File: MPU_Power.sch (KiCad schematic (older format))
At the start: 45 parts, among them U1 STM32MP151AAB3

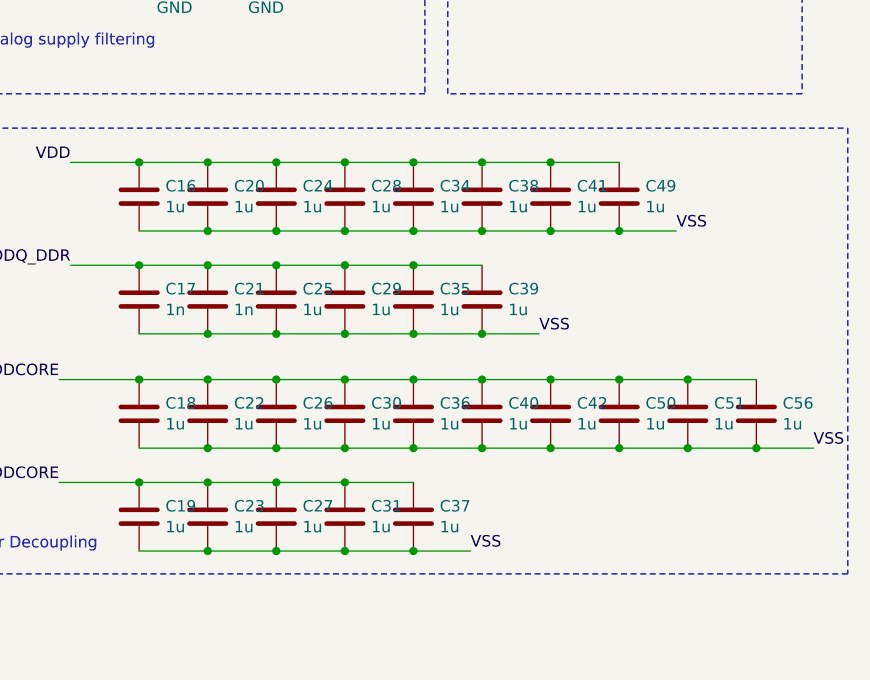
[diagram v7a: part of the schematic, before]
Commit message: Update jtag connector to swd
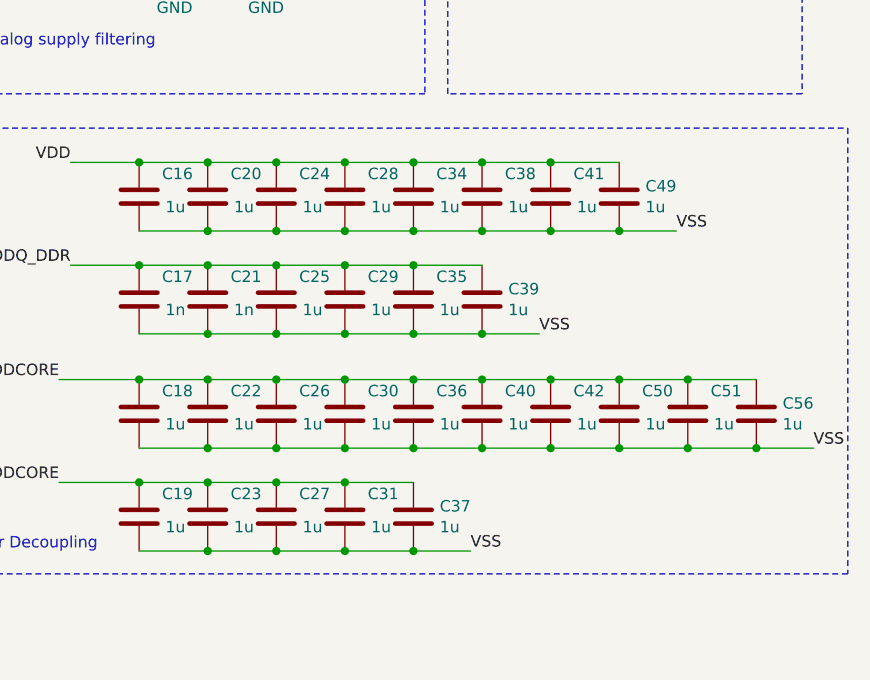
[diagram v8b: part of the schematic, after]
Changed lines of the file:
@@
 U 1 1 60A31F57
 P 8050 5700
-F 0 "C18" H 8165 5746 50  0000 L CNN
+F 0 "C18" H 8150 5800 50  0000 L CNN
 F 1 "1u" H 8165 5655 50  0000 L CNN
 F 2 "Capacitor_SMD:C_0603_1608Metric" H 8088 5550 50  0001 C CNN
@@
 U 1 1 60A5393A
 P 8350 5700
-F 0 "C22" H 8465 5746 50  0000 L CNN
+F 0 "C22" H 8450 5800 50  0000 L CNN
 F 1 "1u" H 8465 5655 50  0000 L CNN
 F 2 "Capacitor_SMD:C_0603_1608Metric" H 8388 5550 50  0001 C CNN
@@
 U 1 1 60A5C6B0
 P 8650 5700
-F 0 "C26" H 8765 5746 50  0000 L CNN
+F 0 "C26" H 8750 5800 50  0000 L CNN
 F 1 "1u" H 8765 5655 50  0000 L CNN
 F 2 "Capacitor_SMD:C_0603_1608Metric" H 8688 5550 50  0001 C CNN
@@
 U 1 1 60A653E0
 P 8950 5700
-F 0 "C30" H 9065 5746 50  0000 L CNN
+F 0 "C30" H 9050 5800 50  0000 L CNN
 F 1 "1u" H 9065 5655 50  0000 L CNN
 F 2 "Capacitor_SMD:C_0603_1608Metric" H 8988 5550 50  0001 C CNN
@@
 U 1 1 60A6E191
 P 9250 5700
-F 0 "C36" H 9365 5746 50  0000 L CNN
+F 0 "C36" H 9350 5800 50  0000 L CNN
 F 1 "1u" H 9365 5655 50  0000 L CNN
 F 2 "Capacitor_SMD:C_0603_1608Metric" H 9288 5550 50  0001 C CNN
@@
 U 1 1 60A76EB4
 P 9550 5700
-F 0 "C40" H 9665 5746 50  0000 L CNN
+F 0 "C40" H 9650 5800 50  0000 L CNN
 F 1 "1u" H 9665 5655 50  0000 L CNN
 F 2 "Capacitor_SMD:C_0603_1608Metric" H 9588 5550 50  0001 C CNN
@@
 U 1 1 60A7FC09
 P 9850 5700
-F 0 "C42" H 9965 5746 50  0000 L CNN
+F 0 "C42" H 9950 5800 50  0000 L CNN
 F 1 "1u" H 9965 5655 50  0000 L CNN
 F 2 "Capacitor_SMD:C_0603_1608Metric" H 9888 5550 50  0001 C CNN
@@
 U 1 1 60A888E7
 P 10150 5700
-F 0 "C50" H 10265 5746 50  0000 L CNN
+F 0 "C50" H 10250 5800 50  0000 L CNN
 F 1 "1u" H 10265 5655 50  0000 L CNN
 F 2 "Capacitor_SMD:C_0603_1608Metric" H 10188 5550 50  0001 C CNN
@@
 U 1 1 60A91686
 P 10450 5700
-F 0 "C51" H 10565 5746 50  0000 L CNN
+F 0 "C51" H 10550 5800 50  0000 L CNN
 F 1 "1u" H 10565 5655 50  0000 L CNN
 F 2 "Capacitor_SMD:C_0603_1608Metric" H 10488 5550 50  0001 C CNN
@@
 	8950 5550 9250 5550
 Connection ~ 9250 5550
-Wire Wire Line
-	9250 5550 9550 5550
 Connection ~ 9550 5550
 Wire Wire Line
@@
 	8950 5850 9250 5850
 Connection ~ 9250 5850
-Wire Wire Line
-	9250 5850 9550 5850
 Connection ~ 9550 5850
 Wire Wire Line
@@
 U 1 1 60AD5BC4
 P 8050 6150
-F 0 "C19" H 8165 6196 50  0000 L CNN
+F 0 "C19" H 8150 6250 50  0000 L CNN
 F 1 "1u" H 8165 6105 50  0000 L CNN
 F 2 "Capacitor_SMD:C_0603_1608Metric" H 8088 6000 50  0001 C CNN
@@
 U 1 1 60AD5BCA
 P 8350 6150
-F 0 "C23" H 8465 6196 50  0000 L CNN
+F 0 "C23" H 8450 6250 50  0000 L CNN
 F 1 "1u" H 8465 6105 50  0000 L CNN
 F 2 "Capacitor_SMD:C_0603_1608Metric" H 8388 6000 50  0001 C CNN
@@
 U 1 1 60AD5BD0
 P 8650 6150
-F 0 "C27" H 8765 6196 50  0000 L CNN
+F 0 "C27" H 8750 6250 50  0000 L CNN
 F 1 "1u" H 8765 6105 50  0000 L CNN
 F 2 "Capacitor_SMD:C_0603_1608Metric" H 8688 6000 50  0001 C CNN
@@
 U 1 1 60AD5BD6
 P 8950 6150
-F 0 "C31" H 9065 6196 50  0000 L CNN
+F 0 "C31" H 9050 6250 50  0000 L CNN
 F 1 "1u" H 9065 6105 50  0000 L CNN
 F 2 "Capacitor_SMD:C_0603_1608Metric" H 8988 6000 50  0001 C CNN
@@
 U 1 1 60B613FA
 P 8050 5200
-F 0 "C17" H 8165 5246 50  0000 L CNN
+F 0 "C17" H 8150 5300 50  0000 L CNN
 F 1 "1n" H 8165 5155 50  0000 L CNN
 F 2 "Capacitor_SMD:C_0603_1608Metric" H 8088 5050 50  0001 C CNN
@@
 U 1 1 60B663B8
 P 8350 5200
-F 0 "C21" H 8465 5246 50  0000 L CNN
+F 0 "C21" H 8450 5300 50  0000 L CNN
 F 1 "1n" H 8465 5155 50  0000 L CNN
 F 2 "Capacitor_SMD:C_0603_1608Metric" H 8388 5050 50  0001 C CNN
@@
 U 1 1 60B715C2
 P 8650 5200
-F 0 "C25" H 8765 5246 50  0000 L CNN
+F 0 "C25" H 8750 5300 50  0000 L CNN
 F 1 "1u" H 8765 5155 50  0000 L CNN
 F 2 "Capacitor_SMD:C_0603_1608Metric" H 8688 5050 50  0001 C CNN
@@
 U 1 1 60B7EB01
 P 8950 5200
-F 0 "C29" H 9065 5246 50  0000 L CNN
+F 0 "C29" H 9050 5300 50  0000 L CNN
 F 1 "1u" H 9065 5155 50  0000 L CNN
 F 2 "Capacitor_SMD:C_0603_1608Metric" H 8988 5050 50  0001 C CNN
@@
 U 1 1 60B88EC8
 P 9250 5200
-F 0 "C35" H 9365 5246 50  0000 L CNN
+F 0 "C35" H 9350 5300 50  0000 L CNN
 F 1 "1u" H 9365 5155 50  0000 L CNN
 F 2 "Capacitor_SMD:C_0603_1608Metric" H 9288 5050 50  0001 C CNN
@@
 Connection ~ 9250 5050
 Wire Wire Line
-	9250 5050 9550 5050
-Wire Wire Line
 	8050 5350 8350 5350
 Connection ~ 8350 5350
@@
 	8950 5350 9250 5350
 Connection ~ 9250 5350
-Wire Wire Line
-	9250 5350 9550 5350
 Wire Wire Line
 	7700 5550 8050 5550
@@
 U 1 1 60DA2B65
 P 8050 4750
-F 0 "C16" H 8165 4796 50  0000 L CNN
+F 0 "C16" H 8150 4850 50  0000 L CNN
 F 1 "1u" H 8165 4705 50  0000 L CNN
 F 2 "Capacitor_SMD:C_0603_1608Metric" H 8088 4600 50  0001 C CNN
@@
 U 1 1 60DA2B6B
 P 8350 4750
-F 0 "C20" H 8465 4796 50  0000 L CNN
+F 0 "C20" H 8450 4850 50  0000 L CNN
 F 1 "1u" H 8465 4705 50  0000 L CNN
 F 2 "Capacitor_SMD:C_0603_1608Metric" H 8388 4600 50  0001 C CNN
@@
 U 1 1 60DA2B71
 P 8650 4750
-F 0 "C24" H 8765 4796 50  0000 L CNN
+F 0 "C24" H 8750 4850 50  0000 L CNN
 F 1 "1u" H 8765 4705 50  0000 L CNN
 F 2 "Capacitor_SMD:C_0603_1608Metric" H 8688 4600 50  0001 C CNN
@@
 U 1 1 60DA2B77
 P 8950 4750
-F 0 "C28" H 9065 4796 50  0000 L CNN
+F 0 "C28" H 9050 4850 50  0000 L CNN
 F 1 "1u" H 9065 4705 50  0000 L CNN
 F 2 "Capacitor_SMD:C_0603_1608Metric" H 8988 4600 50  0001 C CNN
@@
 U 1 1 60E465D3
 P 9250 4750
-F 0 "C34" H 9365 4796 50  0000 L CNN
+F 0 "C34" H 9350 4850 50  0000 L CNN
 F 1 "1u" H 9365 4705 50  0000 L CNN
 F 2 "Capacitor_SMD:C_0603_1608Metric" H 9288 4600 50  0001 C CNN
@@
 U 1 1 60E465D9
 P 9550 4750
-F 0 "C38" H 9665 4796 50  0000 L CNN
+F 0 "C38" H 9650 4850 50  0000 L CNN
 F 1 "1u" H 9665 4705 50  0000 L CNN
 F 2 "Capacitor_SMD:C_0603_1608Metric" H 9588 4600 50  0001 C CNN
@@
 U 1 1 60E465DF
 P 9850 4750
-F 0 "C41" H 9965 4796 50  0000 L CNN
+F 0 "C41" H 9950 4850 50  0000 L CNN
 F 1 "1u" H 9965 4705 50  0000 L CNN
 F 2 "Capacitor_SMD:C_0603_1608Metric" H 9888 4600 50  0001 C CNN
@@
 	3850 4200 3850 4300
 Connection ~ 3850 4300
+Text Label 10450 2200 0    50   ~ 0
+VDD
+Wire Wire Line
+	10100 2200 10450 2200
+Wire Wire Line
+	10100 2700 10450 2700
+Text Label 10450 2700 0    50   ~ 0
+VDD
+Text Label 10450 3200 0    50   ~ 0
+VDD
+Wire Wire Line
+	6450 4000 6450 4200
+Text HLabel 6600 4000 2    50   Input ~ 0
+USB_3V3
+Wire Wire Line
+	6600 4000 6450 4000
+Connection ~ 6450 4000
+Text HLabel 6550 2200 2    50   Input ~ 0
+VDDQ_DDR
+Wire Wire Line
+	6550 2200 6450 2200
+Connection ~ 6450 2200
+Text Label 8200 2400 0    50   ~ 0
+VSS
+$Comp
+L power:GND #PWR0101
+U 1 1 6120E799
+P 8100 2450
+F 0 "#PWR0101" H 8100 2200 50  0001 C CNN
+F 1 "GND" H 8105 2277 50  0000 C CNN
+F 2 "" H 8100 2450 50  0001 C CNN
+F 3 "" H 8100 2450 50  0001 C CNN
+	1    8100 2450
+	1    0    0    -1
+$EndComp
+Wire Wire Line
+	8100 2450 8100 2400
+Wire Wire Line
+	8100 2400 8200 2400
+Wire Wire Line
+	8200 2250 8050 2250
+Text HLabel 6450 3600 2    50   Input ~ 0
+VDDA1V1
+Text HLabel 6450 3800 2    50   Input ~ 0
+VDDA1V8
+Wire Wire Line
+	9250 5850 9550 5850
+Wire Wire Line
+	9250 5550 9550 5550
+Wire Wire Line
+	9250 5350 9550 5350
+Wire Wire Line
+	9250 5050 9550 5050
 $Comp
 L LinuxBoard:STM32MP151AAB3 U?
@@
 	1    0    0    -1
 $EndComp
-Text Label 10450 2200 0    50   ~ 0
-VDD
-Wire Wire Line
-	10100 2200 10450 2200
-Wire Wire Line
-	10100 2700 10450 2700
-Text Label 10450 2700 0    50   ~ 0
-VDD
-Text Label 10450 3200 0    50   ~ 0
-VDD
-Wire Wire Line
-	6450 4000 6450 4200
-Text HLabel 6600 4000 2    50   Input ~ 0
-USB_3V3
-Wire Wire Line
-	6600 4000 6450 4000
-Connection ~ 6450 4000
-Text HLabel 6550 2200 2    50   Input ~ 0
-VDDQ_DDR
-Wire Wire Line
-	6550 2200 6450 2200
-Connection ~ 6450 2200
-Text Label 8200 2400 0    50   ~ 0
-VSS
-$Comp
-L power:GND #PWR0101
-U 1 1 6120E799
-P 8100 2450
-F 0 "#PWR0101" H 8100 2200 50  0001 C CNN
-F 1 "GND" H 8105 2277 50  0000 C CNN
-F 2 "" H 8100 2450 50  0001 C CNN
-F 3 "" H 8100 2450 50  0001 C CNN
-	1    8100 2450
-	1    0    0    -1
-$EndComp
-Wire Wire Line
-	8100 2450 8100 2400
-Wire Wire Line
-	8100 2400 8200 2400
-Wire Wire Line
-	8200 2250 8050 2250
-Text HLabel 6450 3600 2    50   Input ~ 0
-VDDA1V1
-Text HLabel 6450 3800 2    50   Input ~ 0
-VDDA1V8
 $EndSCHEMATC
